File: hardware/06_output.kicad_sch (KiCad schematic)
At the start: 4 parts, among them J2 16-pin IDC POWER OUT

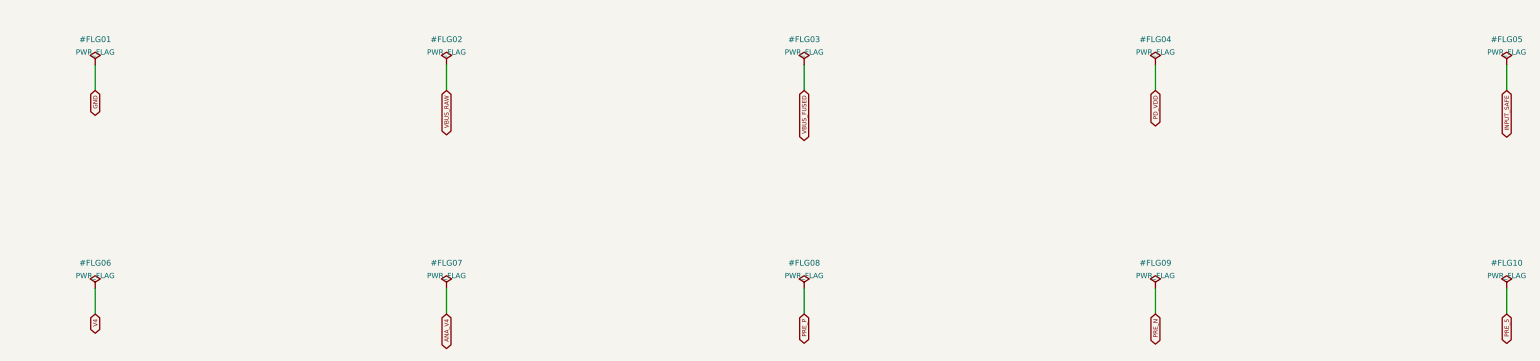
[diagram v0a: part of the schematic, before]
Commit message: Refine USB-C PD input safety review and validate unrouted KiCad prototype
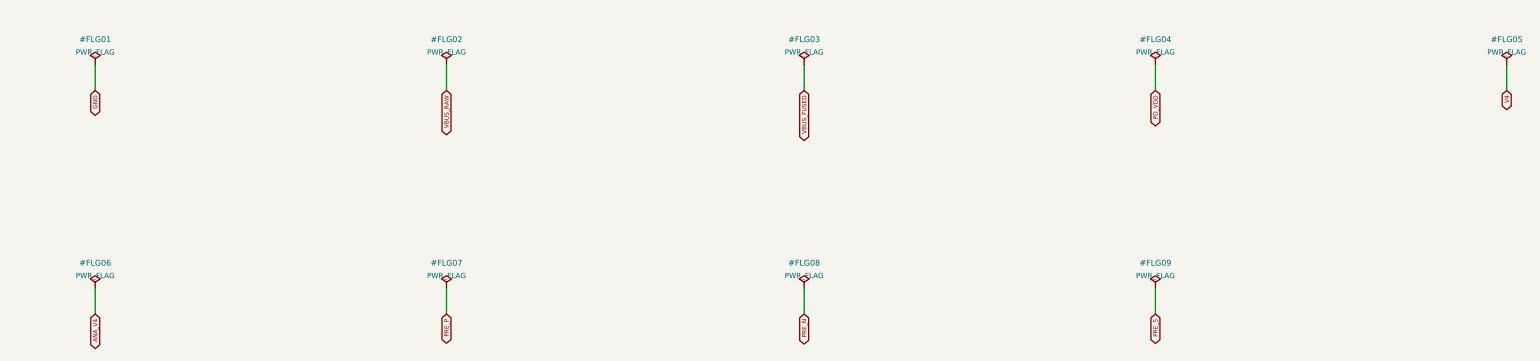
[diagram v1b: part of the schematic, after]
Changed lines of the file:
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@@
 (symbol (lib_id "BigModular:power_PWR_FLAG") (at 260.35 154.94 0) (unit 1) (in_bom no) (on_board yes) (dnp no)(property "Reference" "#FLG04" (at 260.35 149.85999999999999 0) (effects (font (size 1.15 1.15))))(property "Value" "PWR_FLAG" (at 260.35 152.39999999999998 0) (effects (font (size 1.05 1.05))))(property "Footprint" "" (at 260.35 154.94 0) (effects (font (size 1 1)) hide))(property "MPN" "" (at 260.35 154.94 0) (effects (font (size 1 1)) hide))(property "LCSC" "" (at 260.35 154.94 0) (effects (font (size 1 1)) hide))(property "NOTE" "" (at 260.35 154.94 0) (effects (font (size 1 1)) hide))(pin "1")(instances (project "big_modular" (path "/d567704c-57ad-5df1-b183-cadb01fd8972/9268303f-14d9-58fd-b541-631abc3194dd" (reference "#FLG04") (unit 1)))) )
 (wire (pts (xy 330.2 154.94) (xy 330.2 160.02)) (stroke (width 0) (type default)))
-(global_label "INPUT_SAFE" (shape bidirectional) (at 330.2 160.02 270) (effects (font (size 0.85 0.85))))
+(global_label "V4" (shape bidirectional) (at 330.2 160.02 270) (effects (font (size 0.85 0.85))))
 (symbol (lib_id "BigModular:power_PWR_FLAG") (at 330.2 154.94 0) (unit 1) (in_bom no) (on_board yes) (dnp no)(property "Reference" "#FLG05" (at 330.2 149.85999999999999 0) (effects (font (size 1.15 1.15))))(property "Value" "PWR_FLAG" (at 330.2 152.39999999999998 0) (effects (font (size 1.05 1.05))))(property "Footprint" "" (at 330.2 154.94 0) (effects (font (size 1 1)) hide))(property "MPN" "" (at 330.2 154.94 0) (effects (font (size 1 1)) hide))(property "LCSC" "" (at 330.2 154.94 0) (effects (font (size 1 1)) hide))(property "NOTE" "" (at 330.2 154.94 0) (effects (font (size 1 1)) hide))(pin "1")(instances (project "big_modular" (path "/d567704c-57ad-5df1-b183-cadb01fd8972/9268303f-14d9-58fd-b541-631abc3194dd" (reference "#FLG05") (unit 1)))) )
 (wire (pts (xy 49.53 199.39) (xy 49.53 204.47)) (stroke (width 0) (type default)))
-(global_label "V4" (shape bidirectional) (at 49.53 204.47 270) (effects (font (size 0.85 0.85))))
+(global_label "ANA_V4" (shape bidirectional) (at 49.53 204.47 270) (effects (font (size 0.85 0.85))))
 (symbol (lib_id "BigModular:power_PWR_FLAG") (at 49.53 199.39 0) (unit 1) (in_bom no) (on_board yes) (dnp no)(property "Reference" "#FLG06" (at 49.53 194.30999999999997 0) (effects (font (size 1.15 1.15))))(property "Value" "PWR_FLAG" (at 49.53 196.84999999999997 0) (effects (font (size 1.05 1.05))))(property "Footprint" "" (at 49.53 199.39 0) (effects (font (size 1 1)) hide))(property "MPN" "" (at 49.53 199.39 0) (effects (font (size 1 1)) hide))(property "LCSC" "" (at 49.53 199.39 0) (effects (font (size 1 1)) hide))(property "NOTE" "" (at 49.53 199.39 0) (effects (font (size 1 1)) hide))(pin "1")(instances (project "big_modular" (path "/d567704c-57ad-5df1-b183-cadb01fd8972/9268303f-14d9-58fd-b541-631abc3194dd" (reference "#FLG06") (unit 1)))) )
 (wire (pts (xy 119.38 199.39) (xy 119.38 204.47)) (stroke (width 0) (type default)))
-(global_label "ANA_V4" (shape bidirectional) (at 119.38 204.47 270) (effects (font (size 0.85 0.85))))
+(global_label "PRE_P" (shape bidirectional) (at 119.38 204.47 270) (effects (font (size 0.85 0.85))))
 (symbol (lib_id "BigModular:power_PWR_FLAG") (at 119.38 199.39 0) (unit 1) (in_bom no) (on_board yes) (dnp no)(property "Reference" "#FLG07" (at 119.38 194.30999999999997 0) (effects (font (size 1.15 1.15))))(property "Value" "PWR_FLAG" (at 119.38 196.84999999999997 0) (effects (font (size 1.05 1.05))))(property "Footprint" "" (at 119.38 199.39 0) (effects (font (size 1 1)) hide))(property "MPN" "" (at 119.38 199.39 0) (effects (font (size 1 1)) hide))(property "LCSC" "" (at 119.38 199.39 0) (effects (font (size 1 1)) hide))(property "NOTE" "" (at 119.38 199.39 0) (effects (font (size 1 1)) hide))(pin "1")(instances (project "big_modular" (path "/d567704c-57ad-5df1-b183-cadb01fd8972/9268303f-14d9-58fd-b541-631abc3194dd" (reference "#FLG07") (unit 1)))) )
 (wire (pts (xy 190.5 199.39) (xy 190.5 204.47)) (stroke (width 0) (type default)))
-(global_label "PRE_P" (shape bidirectional) (at 190.5 204.47 270) (effects (font (size 0.85 0.85))))
+(global_label "PRE_N" (shape bidirectional) (at 190.5 204.47 270) (effects (font (size 0.85 0.85))))
 (symbol (lib_id "BigModular:power_PWR_FLAG") (at 190.5 199.39 0) (unit 1) (in_bom no) (on_board yes) (dnp no)(property "Reference" "#FLG08" (at 190.5 194.30999999999997 0) (effects (font (size 1.15 1.15))))(property "Value" "PWR_FLAG" (at 190.5 196.84999999999997 0) (effects (font (size 1.05 1.05))))(property "Footprint" "" (at 190.5 199.39 0) (effects (font (size 1 1)) hide))(property "MPN" "" (at 190.5 199.39 0) (effects (font (size 1 1)) hide))(property "LCSC" "" (at 190.5 199.39 0) (effects (font (size 1 1)) hide))(property "NOTE" "" (at 190.5 199.39 0) (effects (font (size 1 1)) hide))(pin "1")(instances (project "big_modular" (path "/d567704c-57ad-5df1-b183-cadb01fd8972/9268303f-14d9-58fd-b541-631abc3194dd" (reference "#FLG08") (unit 1)))) )
 (wire (pts (xy 260.35 199.39) (xy 260.35 204.47)) (stroke (width 0) (type default)))
-(global_label "PRE_N" (shape bidirectional) (at 260.35 204.47 270) (effects (font (size 0.85 0.85))))
+(global_label "PRE_5" (shape bidirectional) (at 260.35 204.47 270) (effects (font (size 0.85 0.85))))
 (symbol (lib_id "BigModular:power_PWR_FLAG") (at 260.35 199.39 0) (unit 1) (in_bom no) (on_board yes) (dnp no)(property "Reference" "#FLG09" (at 260.35 194.30999999999997 0) (effects (font (size 1.15 1.15))))(property "Value" "PWR_FLAG" (at 260.35 196.84999999999997 0) (effects (font (size 1.05 1.05))))(property "Footprint" "" (at 260.35 199.39 0) (effects (font (size 1 1)) hide))(property "MPN" "" (at 260.35 199.39 0) (effects (font (size 1 1)) hide))(property "LCSC" "" (at 260.35 199.39 0) (effects (font (size 1 1)) hide))(property "NOTE" "" (at 260.35 199.39 0) (effects (font (size 1 1)) hide))(pin "1")(instances (project "big_modular" (path "/d567704c-57ad-5df1-b183-cadb01fd8972/9268303f-14d9-58fd-b541-631abc3194dd" (reference "#FLG09") (unit 1)))) )
-(wire (pts (xy 330.2 199.39) (xy 330.2 204.47)) (stroke (width 0) (type default)))
-(global_label "PRE_5" (shape bidirectional) (at 330.2 204.47 270) (effects (font (size 0.85 0.85))))
-(symbol (lib_id "BigModular:power_PWR_FLAG") (at 330.2 199.39 0) (unit 1) (in_bom no) (on_board yes) (dnp no)(property "Reference" "#FLG10" (at 330.2 194.30999999999997 0) (effects (font (size 1.15 1.15))))(property "Value" "PWR_FLAG" (at 330.2 196.84999999999997 0) (effects (font (size 1.05 1.05))))(property "Footprint" "" (at 330.2 199.39 0) (effects (font (size 1 1)) hide))(property "MPN" "" (at 330.2 199.39 0) (effects (font (size 1 1)) hide))(property "LCSC" "" (at 330.2 199.39 0) (effects (font (size 1 1)) hide))(property "NOTE" "" (at 330.2 199.39 0) (effects (font (size 1 1)) hide))(pin "1")(instances (project "big_modular" (path "/d567704c-57ad-5df1-b183-cadb01fd8972/9268303f-14d9-58fd-b541-631abc3194dd" (reference "#FLG10") (unit 1)))) )
 (embedded_fonts no))
